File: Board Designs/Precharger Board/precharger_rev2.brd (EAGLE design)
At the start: 84.8 x 52.1 mm, 21 parts, among them X1 CONNECTOR-2, X2 CONNECTOR-2

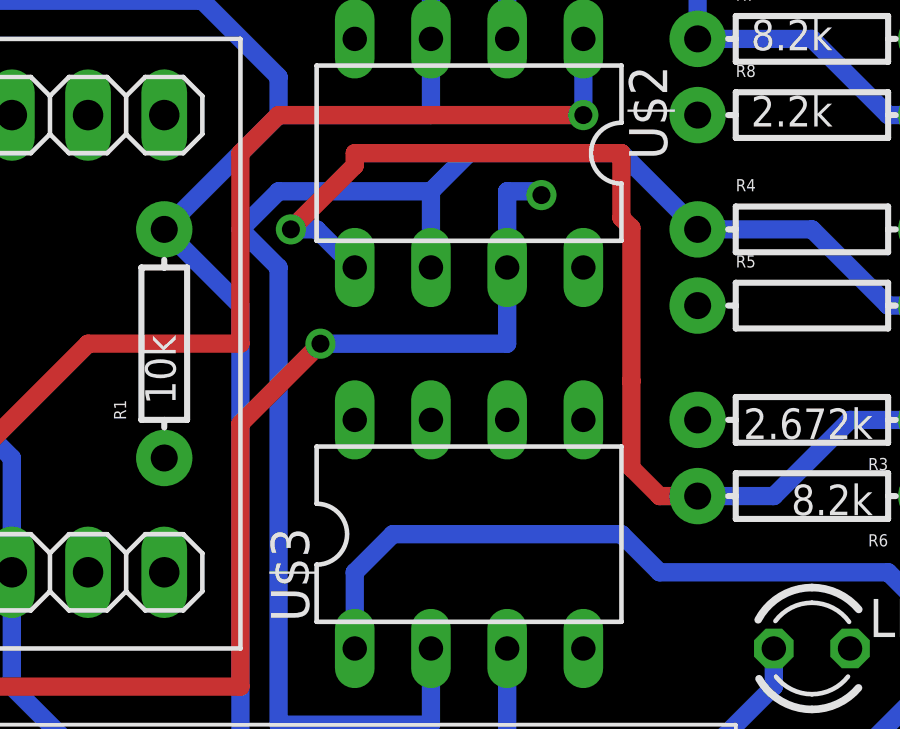
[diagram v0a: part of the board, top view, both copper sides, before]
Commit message: Revised precharger design
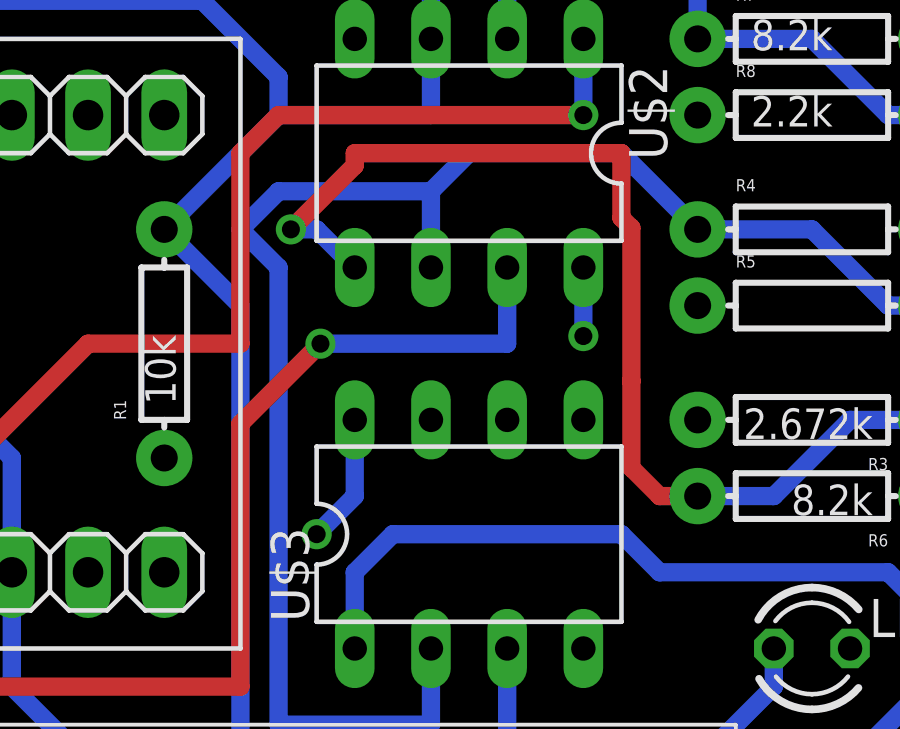
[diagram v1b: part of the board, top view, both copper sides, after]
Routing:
- net VIN: track 30.9 -> 37.5 mm, vias 2 -> 4
- net N$5: track 41.5 -> 37.8 mm, vias 3 -> 2
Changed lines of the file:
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@@
 <wire x1="72.18" y1="50.59" x2="71.12" y2="49.53" width="0.6096" layer="16"/>
 <via x="71.12" y="49.53" extent="1-16" drill="0.6"/>
+<wire x1="49.53" y1="53.34" x2="49.53" y2="50.8" width="0.6096" layer="16"/>
+<wire x1="49.53" y1="50.8" x2="48.26" y2="49.53" width="0.6096" layer="16"/>
+<via x="48.26" y="49.53" extent="1-16" drill="0.6"/>
+<wire x1="57.15" y1="58.42" x2="57.15" y2="56.134" width="0.6096" layer="16"/>
+<via x="57.15" y="56.134" extent="1-16" drill="0.6"/>
 </signal>
 <signal name="N$6">
@@
 <contactref element="U$2" pad="7"/>
 <contactref element="U$1" pad="12"/>
-<wire x1="54.61" y1="58.42" x2="54.61" y2="60.96" width="0.6096" layer="16"/>
-<wire x1="54.61" y1="60.96" x2="55.626" y2="60.96" width="0.6096" layer="16"/>
-<wire x1="55.626" y1="60.96" x2="55.753" y2="60.833" width="0.6096" layer="16"/>
-<via x="55.753" y="60.833" extent="1-16" drill="0.6"/>
 <wire x1="54.61" y1="58.42" x2="54.61" y2="55.88" width="0.6096" layer="16"/>
 <wire x1="54.61" y1="55.88" x2="48.387" y2="55.88" width="0.6096" layer="16"/>
